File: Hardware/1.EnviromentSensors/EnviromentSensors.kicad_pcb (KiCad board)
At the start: 2 copper layers, 70 x 70 mm, 14 parts, among them J2 Conn_01x05_Pin, U1 SHT4x, U2 BME680, U3 LPS22HB

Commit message: Change PCB design
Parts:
- JP1, JP2: moved to B.Cu
- moved JP1 13.7 mm to (143.7, 75.3), turned to -90 degrees
- moved JP2 12.7 mm to (143.7, 81.4), turned to -90 degrees
- moved J2 12.3 mm to (131.3, 112.8)
- moved R1 6.90 mm to (133.3, 85.9)
- moved R4 1.58 mm to (142.6, 92.7), turned to 180 degrees
- moved R2 1.29 mm to (136.8, 87.2)
- moved R3 1.29 mm to (134.2, 87.3)
- moved C1 0.78 mm to (133.7, 74.4)
- moved U2 0.78 mm to (136.2, 75.5)
- moved C2 0.78 mm to (133.7, 76.5)
- moved C3 0.59 mm to (146.1, 90.5)
- moved U3 0.57 mm to (143.9, 90.5)
- moved U1 0.57 mm to (126.7, 90.5)
- moved C4 0.21 mm to (144.3, 88.2), turned to 180 degrees
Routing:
- net Net-(JP1-B): track 9.37 -> 26.2 mm, vias 0 -> 1
- net I2C_SDA: track 41.8 -> 54.9 mm, vias 0 -> 2
- net I2C_SCL: track 44.2 -> 57.2 mm, vias 3 -> 2
- net LPS22HB_INT: track 14.4 -> 25.0 mm
- net GND: track 9.77 -> 19.1 mm, vias 0 -> 1
- net Net-(JP2-B): track 6.88 -> 15.1 mm, vias 0 -> 1
- net +3.3V: track 27.6 -> 31.9 mm, vias 7 -> 6
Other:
- outline, holes or cut-outs redrawn
- board text added: "."
- board text added: "1"
- board text added: "BME680 Address: 0x76 - Closed 0x77 - Open"
- board text added: "LPS22HB Address: 0x5C - Closed 0x5D - Open"

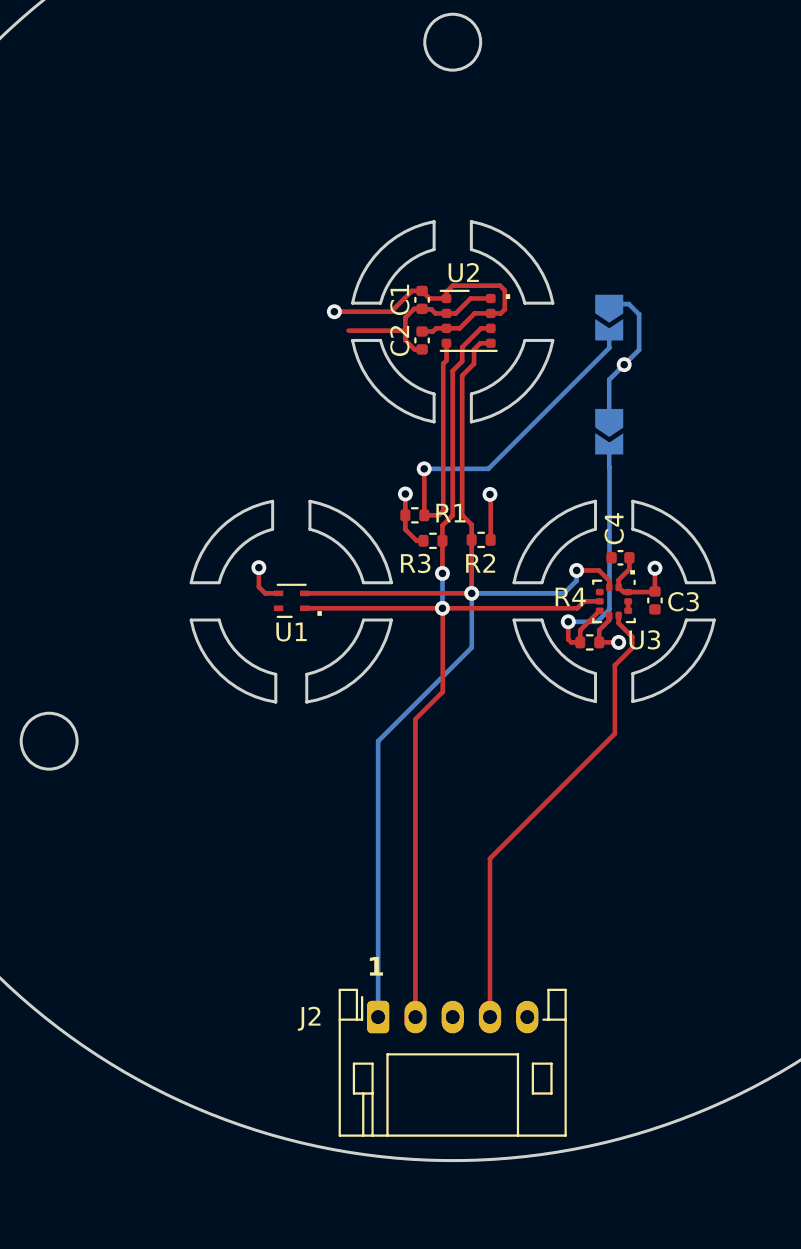
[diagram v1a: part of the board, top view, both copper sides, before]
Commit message: Update PCB by adding connector for LightSensors board
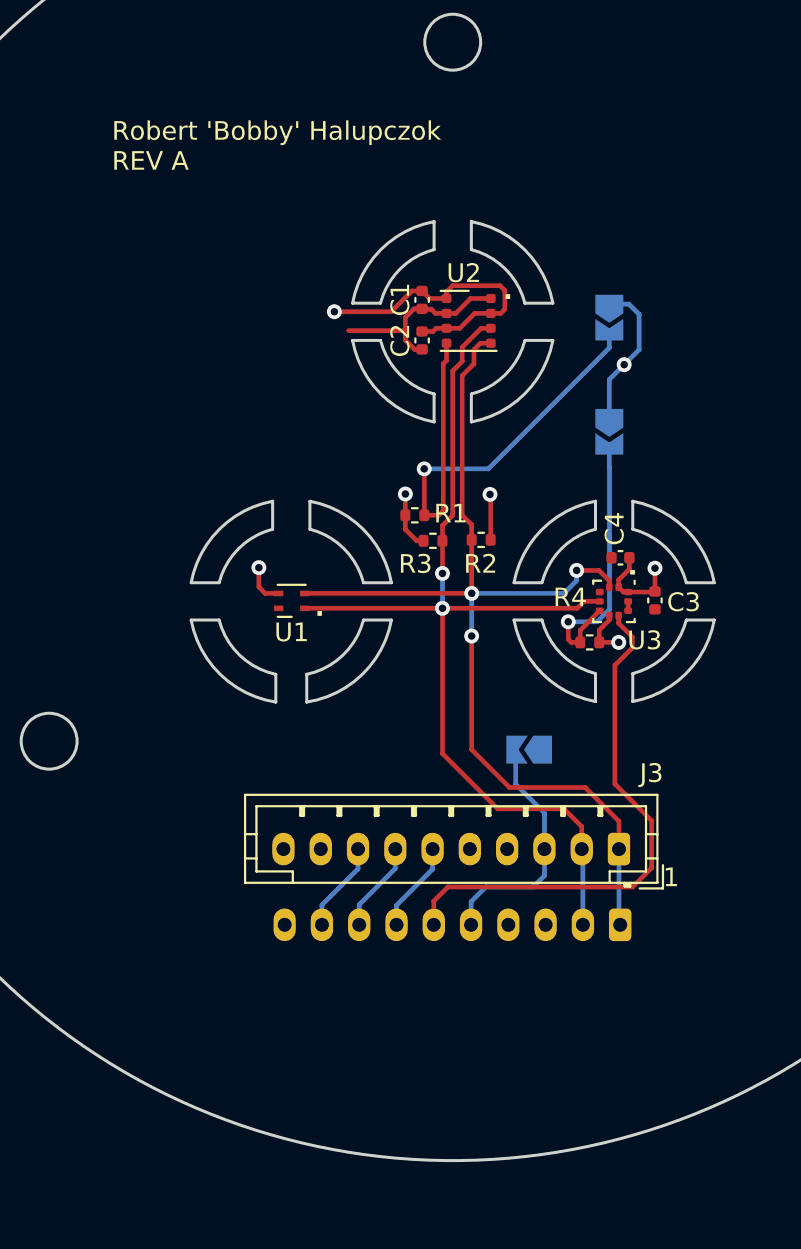
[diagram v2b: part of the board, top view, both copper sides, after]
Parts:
- removed J2: Conn_01x05_Pin, Connector_JST:JST_PH_S5B-PH-K_1x05_P2.00mm_Horizontal
- added J1: Conn_01x10_Pin, Connector_JST:JST_PH_S10B-PH-K_1x10_P2.00mm_Horizontal, B.Cu at (144.3, 107.9)
- added J3: Conn_01x10_Pin, Connector_JST:JST_PH_B10B-PH-K_1x10_P2.00mm_Vertical, F.Cu at (144.2, 103.8)
- added JP3: SolderJumper_2_Open, Jumper:SolderJumper-2_P1.3mm_Open_TrianglePad1.0x1.5mm, B.Cu at (139.4, 98.5)
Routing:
- net EXT_3V3: track 0.00 -> 13.2 mm
- net EXT_AS7331_READY: track 0.00 -> 4.87 mm
- net EXT_OPT3004_INT: track 0.00 -> 4.87 mm
- net EXT_AS7331_SYN: track 0.00 -> 4.87 mm
- net LPS22HB_INT: track 25.0 -> 28.7 mm
- net I2C_SCL: track 57.2 -> 55.7 mm, vias 2 -> 3
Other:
- board text added: "Robert 'Bobby' Halupczok REV A"
- board text added: "SHT45 Address: SHT4x-A - 0x44 SHT4x-B - 0x45 SHT4x-C - 0x46"
